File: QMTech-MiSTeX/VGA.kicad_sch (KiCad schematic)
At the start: 7 parts

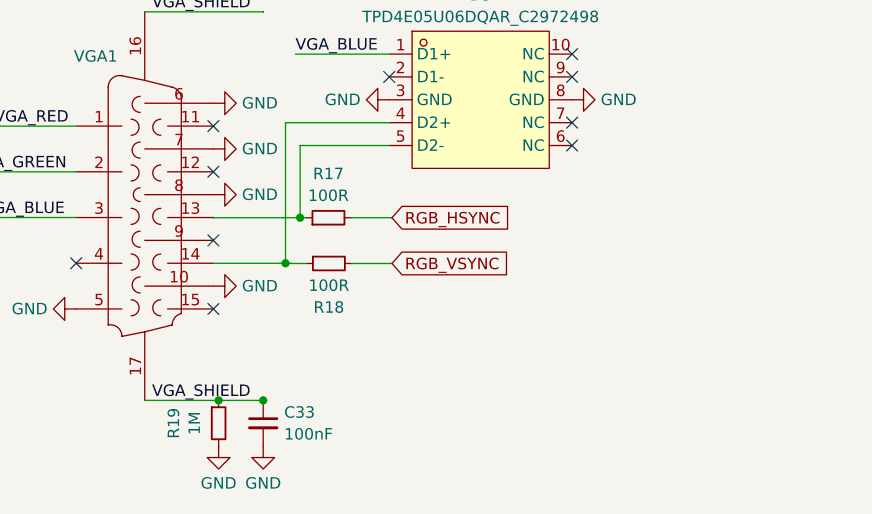
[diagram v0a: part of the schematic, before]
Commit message: apply review notes from somhi, move audio into its own subsheet, add analog audio out
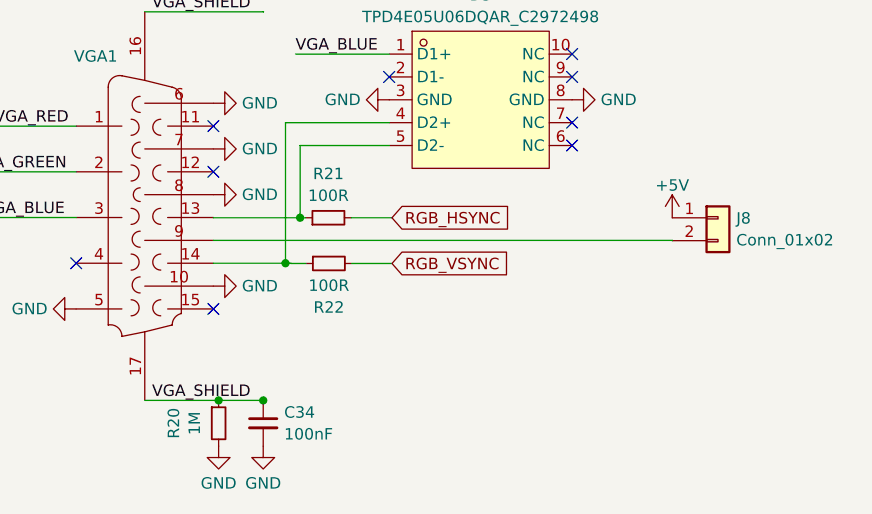
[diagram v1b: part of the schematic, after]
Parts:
- added J8: Conn_01x02, Connector_PinHeader_1.00mm:PinHeader_1x02_P1.00mm_Vertical, symbol Connector_Generic:Conn_01x02
- renumbered C33 to C34, R19 to R20, R17 to R21, R18 to R22
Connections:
- net at VGA1.9: now also J8.2 (Pin_2)
- new net +5V: J8.1 (Pin_1)
- no-connect marks 16 -> 15
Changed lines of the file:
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@@
   (no_connect (at 152.1599 119.3546))
   (no_connect (at 155.4988 89.8652))
-  (no_connect (at 152.1599 126.9746))
   (no_connect (at 155.4988 79.7052))
   (no_connect (at 192.024 106.2736))
@@
     (stroke (width 0) (type default))
   )
+  (wire (pts (xy 152.1599 126.9746) (xy 203.1506 126.9746))
+    (stroke (width 0) (type default))
+  )
   (wire (pts (xy 79.6036 91.1606) (xy 79.6036 91.2876))
     (stroke (width 0) (type default))
@@
     (stroke (width 0) (type default))
   )
+  (wire (pts (xy 203.1506 126.9746) (xy 203.1506 127.0057))
+    (stroke (width 0) (type default))
+  )
   (wire (pts (xy 79.6036 139.4206) (xy 79.6036 139.6746))
     (stroke (width 0) (type default))
@@
     )
   )
+  (symbol (lib_id "power:+5V") (at 203.1506 124.4657 0) (unit 1)
+    (in_bom yes) (on_board yes) (dnp no) (fields_autoplaced)
+    (property "Reference" "#PWR0110" (at 203.1506 128.2757 0)
+      (effects (font (size 1.27 1.27)) hide)
+    )
+    (property "Value" "+5V" (at 203.1506 120.8611 0)
+      (effects (font (size 1.27 1.27)))
+    )
+    (property "Footprint" "" (at 203.1506 124.4657 0)
+      (effects (font (size 1.27 1.27)) hide)
+    )
+    (property "Datasheet" "" (at 203.1506 124.4657 0)
+      (effects (font (size 1.27 1.27)) hide)
+    )
+    (pin "1")
+    (instances
+      (project "QMTech-MiSTeX"
+        (path "/bf95850e-2fcb-4784-a603-f17fc357556b/8c1d97fc-c85e-4afc-840e-7429a199eff3"
+          (reference "#PWR0110") (unit 1)
+        )
+      )
+    )
+  )
   (symbol (lib_id "power:GND") (at 157.7007 149.8346 0) (unit 1)
     (in_bom yes) (on_board yes) (dnp no) (fields_autoplaced)
-    (property "Reference" "#PWR099" (at 157.7007 156.1846 0)
+    (property "Reference" "#PWR0107" (at 157.7007 156.1846 0)
       (effects (font (size 1.27 1.27)) hide)
     )
@@
       (project "QMTech-MiSTeX"
         (path "/bf95850e-2fcb-4784-a603-f17fc357556b/8c1d97fc-c85e-4afc-840e-7429a199eff3"
-          (reference "#PWR099") (unit 1)
+          (reference "#PWR0107") (unit 1)
         )
       )
@@
   (symbol (lib_id "power:GND") (at 123.4948 84.7852 270) (mirror x) (unit 1)
     (in_bom yes) (on_board yes) (dnp no)
-    (property "Reference" "#PWR0108" (at 117.1448 84.7852 0)
+    (property "Reference" "#PWR099" (at 117.1448 84.7852 0)
       (effects (font (size 1.27 1.27)) hide)
     )
@@
       (project "QMTech-MiSTeX"
         (path "/bf95850e-2fcb-4784-a603-f17fc357556b/8c1d97fc-c85e-4afc-840e-7429a199eff3"
-          (reference "#PWR0108") (unit 1)
+          (reference "#PWR099") (unit 1)
         )
       )
@@
   (symbol (lib_id "power:GND") (at 152.1599 111.7346 90) (unit 1)
     (in_bom yes) (on_board yes) (dnp no) (fields_autoplaced)
-    (property "Reference" "#PWR094" (at 158.5099 111.7346 0)
+    (property "Reference" "#PWR0101" (at 158.5099 111.7346 0)
       (effects (font (size 1.27 1.27)) hide)
     )
@@
       (project "QMTech-MiSTeX"
         (path "/bf95850e-2fcb-4784-a603-f17fc357556b/8c1d97fc-c85e-4afc-840e-7429a199eff3"
-          (reference "#PWR094") (unit 1)
+          (reference "#PWR0101") (unit 1)
         )
       )
@@
   (symbol (lib_id "power:GND") (at 152.7482 149.8346 0) (unit 1)
     (in_bom yes) (on_board yes) (dnp no) (fields_autoplaced)
-    (property "Reference" "#PWR0100" (at 152.7482 156.1846 0)
+    (property "Reference" "#PWR0105" (at 152.7482 156.1846 0)
       (effects (font (size 1.27 1.27)) hide)
     )
@@
       (project "QMTech-MiSTeX"
         (path "/bf95850e-2fcb-4784-a603-f17fc357556b/8c1d97fc-c85e-4afc-840e-7429a199eff3"
-          (reference "#PWR0100") (unit 1)
+          (reference "#PWR0105") (unit 1)
         )
       )
@@
   (symbol (lib_id "jlcpcb-basic-mlcc-0402:100nF") (at 157.7007 147.2946 0) (unit 1)
     (in_bom yes) (on_board yes) (dnp no)
-    (property "Reference" "C33" (at 160.0248 146.0888 0)
+    (property "Reference" "C34" (at 160.0248 146.0888 0)
       (effects (font (size 1.27 1.27)) (justify left))
     )
@@
       (project "QMTech-MiSTeX"
         (path "/bf95850e-2fcb-4784-a603-f17fc357556b/8c1d97fc-c85e-4afc-840e-7429a199eff3"
-          (reference "C33") (unit 1)
+          (reference "C34") (unit 1)
+        )
+      )
+    )
+  )
+  (symbol (lib_id "Connector_Generic:Conn_01x02") (at 208.2306 124.4657 0) (unit 1)
+    (in_bom yes) (on_board yes) (dnp no) (fields_autoplaced)
+    (property "Reference" "J8" (at 210.2626 124.5236 0)
+      (effects (font (size 1.27 1.27)) (justify left))
+    )
+    (property "Value" "Conn_01x02" (at 210.2626 126.9478 0)
+      (effects (font (size 1.27 1.27)) (justify left))
+    )
+    (property "Footprint" "Connector_PinHeader_1.00mm:PinHeader_1x02_P1.00mm_Vertical" (at 208.2306 124.4657 0)
+      (effects (font (size 1.27 1.27)) hide)
+    )
+    (property "Datasheet" "~" (at 208.2306 124.4657 0)
+      (effects (font (size 1.27 1.27)) hide)
+    )
+    (pin "2")
+    (pin "1")
+    (instances
+      (project "QMTech-MiSTeX"
+        (path "/bf95850e-2fcb-4784-a603-f17fc357556b/8c1d97fc-c85e-4afc-840e-7429a199eff3"
+          (reference "J8") (unit 1)
         )
       )
@@
   (symbol (lib_id "Device:R_Small") (at 152.7482 147.2946 0) (unit 1)
     (in_bom yes) (on_board yes) (dnp no)
-    (property "Reference" "R19" (at 147.7698 147.2946 90)
+    (property "Reference" "R20" (at 147.7698 147.2946 90)
       (effects (font (size 1.27 1.27)))
     )
@@
       (project "QMTech-MiSTeX"
         (path "/bf95850e-2fcb-4784-a603-f17fc357556b/8c1d97fc-c85e-4afc-840e-7429a199eff3"
-          (reference "R19") (unit 1)
+          (reference "R20") (unit 1)
         )
       )
@@
   (symbol (lib_id "jlcpcb-basic-resistor-0402:100R") (at 164.9476 124.46 90) (unit 1)
     (in_bom yes) (on_board yes) (dnp no) (fields_autoplaced)
-    (property "Reference" "R17" (at 164.9476 119.5791 90)
+    (property "Reference" "R21" (at 164.9476 119.5791 90)
       (effects (font (size 1.27 1.27)))
     )
@@
       (project "QMTech-MiSTeX"
         (path "/bf95850e-2fcb-4784-a603-f17fc357556b/8c1d97fc-c85e-4afc-840e-7429a199eff3"
-          (reference "R17") (unit 1)
+          (reference "R21") (unit 1)
         )
       )
@@
   (symbol (lib_id "power:GND") (at 152.1599 121.8946 90) (unit 1)
     (in_bom yes) (on_board yes) (dnp no) (fields_autoplaced)
-    (property "Reference" "#PWR096" (at 158.5099 121.8946 0)
+    (property "Reference" "#PWR0103" (at 158.5099 121.8946 0)
       (effects (font (size 1.27 1.27)) hide)
     )
@@
       (project "QMTech-MiSTeX"
         (path "/bf95850e-2fcb-4784-a603-f17fc357556b/8c1d97fc-c85e-4afc-840e-7429a199eff3"
-          (reference "#PWR096") (unit 1)
+          (reference "#PWR0103") (unit 1)
         )
       )
@@
   (symbol (lib_id "power:GND") (at 171.704 111.3536 270) (mirror x) (unit 1)
     (in_bom yes) (on_board yes) (dnp no)
-    (property "Reference" "#PWR0110" (at 165.354 111.3536 0)
+    (property "Reference" "#PWR0108" (at 165.354 111.3536 0)
       (effects (font (size 1.27 1.27)) hide)
     )
@@
       (project "QMTech-MiSTeX"
         (path "/bf95850e-2fcb-4784-a603-f17fc357556b/8c1d97fc-c85e-4afc-840e-7429a199eff3"
-          (reference "#PWR0110") (unit 1)
+          (reference "#PWR0108") (unit 1)
         )
       )
@@
   (symbol (lib_id "power:GND") (at 155.4988 84.7852 90) (unit 1)
     (in_bom yes) (on_board yes) (dnp no) (fields_autoplaced)
-    (property "Reference" "#PWR0107" (at 161.8488 84.7852 0)
+    (property "Reference" "#PWR0106" (at 161.8488 84.7852 0)
       (effects (font (size 1.27 1.27)) hide)
     )
@@
       (project "QMTech-MiSTeX"
         (path "/bf95850e-2fcb-4784-a603-f17fc357556b/8c1d97fc-c85e-4afc-840e-7429a199eff3"
-          (reference "#PWR0107") (unit 1)
+          (reference "#PWR0106") (unit 1)
         )
       )
@@
   (symbol (lib_id "power:GND") (at 152.1599 132.0546 90) (unit 1)
     (in_bom yes) (on_board yes) (dnp no) (fields_autoplaced)
-    (property "Reference" "#PWR097" (at 158.5099 132.0546 0)
+    (property "Reference" "#PWR0104" (at 158.5099 132.0546 0)
       (effects (font (size 1.27 1.27)) hide)
     )
@@
       (project "QMTech-MiSTeX"
         (path "/bf95850e-2fcb-4784-a603-f17fc357556b/8c1d97fc-c85e-4afc-840e-7429a199eff3"
-          (reference "#PWR097") (unit 1)
+          (reference "#PWR0104") (unit 1)
         )
       )
@@
   (symbol (lib_id "power:GND") (at 136.9199 134.5946 270) (mirror x) (unit 1)
     (in_bom yes) (on_board yes) (dnp no)
-    (property "Reference" "#PWR098" (at 130.5699 134.5946 0)
+    (property "Reference" "#PWR0100" (at 130.5699 134.5946 0)
       (effects (font (size 1.27 1.27)) hide)
     )
@@
       (project "QMTech-MiSTeX"
         (path "/bf95850e-2fcb-4784-a603-f17fc357556b/8c1d97fc-c85e-4afc-840e-7429a199eff3"
-          (reference "#PWR098") (unit 1)
+          (reference "#PWR0100") (unit 1)
         )
       )
@@
   (symbol (lib_id "jlcpcb-basic-resistor-0402:100R") (at 164.9984 129.54 90) (mirror x) (unit 1)
     (in_bom yes) (on_board yes) (dnp no)
-    (property "Reference" "R18" (at 164.9984 134.4209 90)
+    (property "Reference" "R22" (at 164.9984 134.4209 90)
       (effects (font (size 1.27 1.27)))
     )
@@
       (project "QMTech-MiSTeX"
         (path "/bf95850e-2fcb-4784-a603-f17fc357556b/8c1d97fc-c85e-4afc-840e-7429a199eff3"
-          (reference "R18") (unit 1)
+          (reference "R22") (unit 1)
         )
       )
@@
   (symbol (lib_id "power:GND") (at 152.1599 116.8146 90) (unit 1)
     (in_bom yes) (on_board yes) (dnp no) (fields_autoplaced)
-    (property "Reference" "#PWR095" (at 158.5099 116.8146 0)
+    (property "Reference" "#PWR0102" (at 158.5099 116.8146 0)
       (effects (font (size 1.27 1.27)) hide)
     )
@@
       (project "QMTech-MiSTeX"
         (path "/bf95850e-2fcb-4784-a603-f17fc357556b/8c1d97fc-c85e-4afc-840e-7429a199eff3"
-          (reference "#PWR095") (unit 1)
+          (reference "#PWR0102") (unit 1)
         )
       )

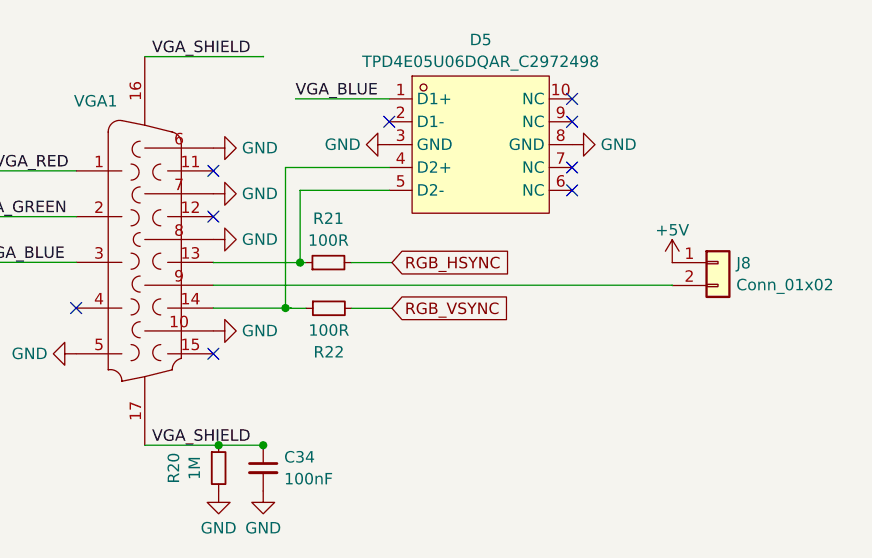
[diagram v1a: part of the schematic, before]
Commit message: finish routing/layouting, fix silk screen, add mounting holes
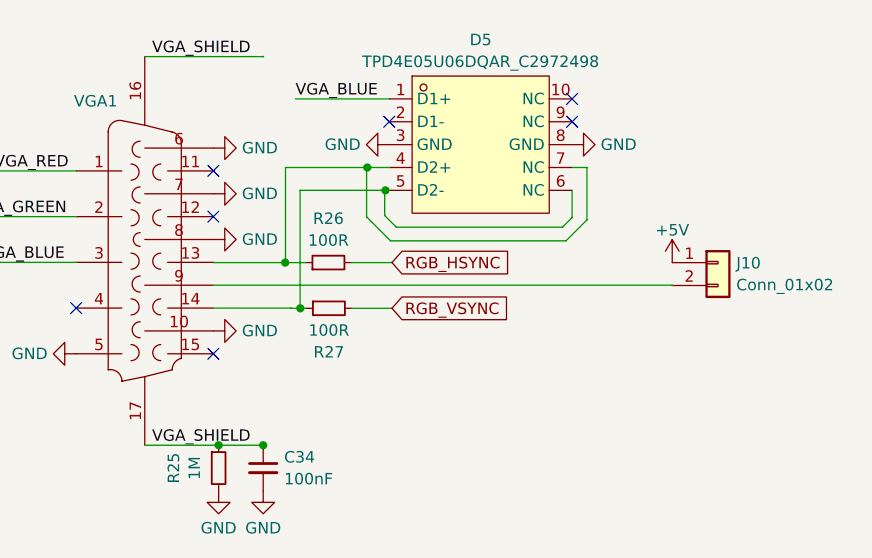
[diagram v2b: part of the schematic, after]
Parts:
- J10: renamed from J8; footprint Connector_PinHeader_1.00mm:PinHeader_1x02_P1.00mm_Vertical -> Connector_PinHeader_2.54mm:PinHeader_1x02_P2.54mm_Vertical
- renumbered R20 to R25, R21 to R26, R22 to R27
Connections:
- net at R26.1, VGA1.13: now also D5.4 (D2+), D5.7 (NC); no longer D5.5 (D2-)
- net at R27.1, VGA1.14: now also D5.5 (D2-), D5.6 (NC); no longer D5.4 (D2+)
- no-connect marks 15 -> 13
